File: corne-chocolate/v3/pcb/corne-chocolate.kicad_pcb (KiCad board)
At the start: 2 copper layers, 275.5 x 105.6 mm, 154 parts, among them J1 MJ-4PP-9, J2 OLED, J3 MJ-4PP-9, J4 OLED, SW10 SW_PUSH, SW11 SW_PUSH, SW12 SW_PUSH, SW14 SW_PUSH, SW15 SW_PUSH, SW16 SW_PUSH, SW17 SW_PUSH, SW18 SW_PUSH, SW19 SW_PUSH, SW2 SW_PUSH, SW20 SW_PUSH, SW21 SW_PUSH, SW23 SW_PUSH, SW24 SW_PUSH, SW25 SW_PUSH, SW26 SW_PUSH, SW27 SW_PUSH, SW29 SW_PUSH, SW3 SW_PUSH, SW30 SW_PUSH, SW31 SW_PUSH, SW32 SW_PUSH, SW33 SW_PUSH, SW35 SW_PUSH, SW36 SW_PUSH, SW37 SW_PUSH, SW38 SW_PUSH, SW39 SW_PUSH, SW4 SW_PUSH, SW40 SW_PUSH, SW41 SW_PUSH, SW42 SW_PUSH, SW5 SW_PUSH, SW6 SW_PUSH, SW8 SW_PUSH, SW9 SW_PUSH, U1 ProMicro, U2 ProMicro

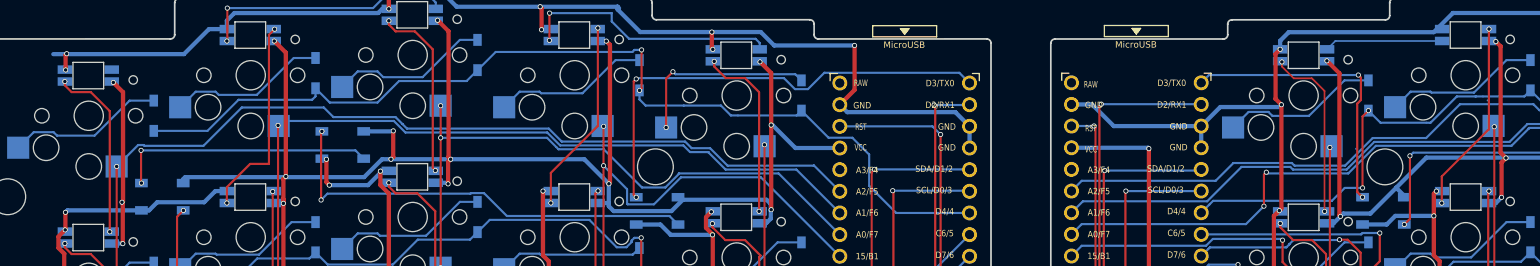
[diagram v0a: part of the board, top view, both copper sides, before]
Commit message: Fix incorrect connections
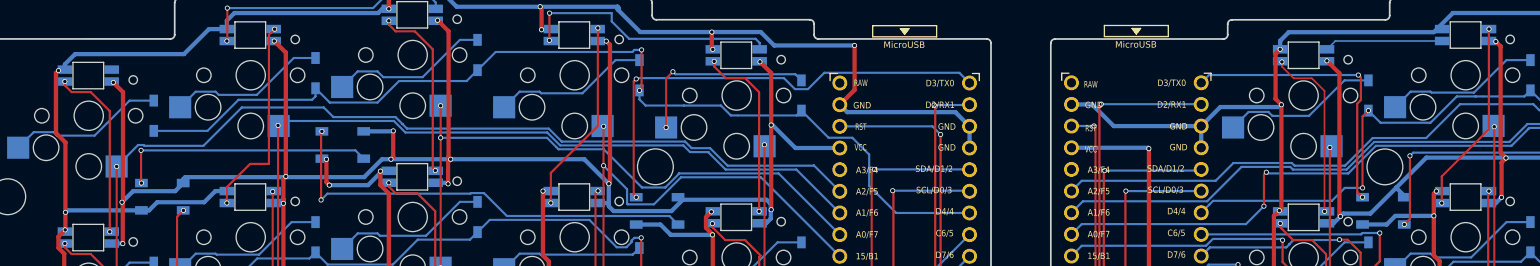
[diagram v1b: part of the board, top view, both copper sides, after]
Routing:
- net GND: track 507.1 -> 522.1 mm, vias 35 -> 34
- net VCC: track 427.1 -> 435.2 mm
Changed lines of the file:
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@@
     (thickness 1.6)
     (drawings 605)
-    (tracks 1983)
+    (tracks 1987)
     (zones 0)
     (modules 154)
@@
     (0 F.Cu signal)
     (31 B.Cu signal)
-    (32 B.Adhes user)
-    (33 F.Adhes user)
-    (34 B.Paste user)
-    (35 F.Paste user)
-    (36 B.SilkS user)
-    (37 F.SilkS user)
-    (38 B.Mask user)
-    (39 F.Mask user)
-    (40 Dwgs.User user)
+    (32 B.Adhes user hide)
+    (33 F.Adhes user hide)
+    (34 B.Paste user hide)
+    (35 F.Paste user hide)
+    (36 B.SilkS user hide)
+    (37 F.SilkS user hide)
+    (38 B.Mask user hide)
+    (39 F.Mask user hide)
+    (40 Dwgs.User user hide)
     (41 Cmts.User user hide)
-    (42 Eco1.User user)
-    (43 Eco2.User user)
-    (44 Edge.Cuts user)
-    (45 Margin user)
-    (46 B.CrtYd user)
-    (47 F.CrtYd user)
-    (48 B.Fab user)
+    (42 Eco1.User user hide)
+    (43 Eco2.User user hide)
+    (44 Edge.Cuts user hide)
+    (45 Margin user hide)
+    (46 B.CrtYd user hide)
+    (47 F.CrtYd user hide)
+    (48 B.Fab user hide)
     (49 F.Fab user hide)
   )
@@
     (effects (font (size 1 1) (thickness 0.125)) (justify left))
   )
+  (via (at 35.56 30.48) (size 0.6) (drill 0.4) (layers F.Cu B.Cu) (net 23))
   (segment (start 122.7075 35.18) (end 122.143681 35.743819) (width 0.25) (layer B.Cu) (net 1))
   (segment (start 103.7075 33.86996) (end 103.7075 32.805) (width 0.25) (layer B.Cu) (net 1))
@@
   (segment (start 108.54522 65.35736) (end 111.6731 65.35736) (width 0.5) (layer B.Cu) (net 23))
   (segment (start 105.44381 62.25595) (end 108.54522 65.35736) (width 0.5) (layer B.Cu) (net 23))
-  (via (at 36.39398 30.40696) (size 0.6) (drill 0.4) (layers F.Cu B.Cu) (net 23))
-  (segment (start 36.35298 30.36596) (end 36.39398 30.40696) (width 0.5) (layer B.Cu) (net 23))
   (segment (start 36.3067 30.36596) (end 36.35298 30.36596) (width 0.5) (layer B.Cu) (net 23))
-  (via (at 36.5218 28.50195) (size 0.6) (drill 0.4) (layers F.Cu B.Cu) (net 23))
-  (segment (start 36.39398 28.62977) (end 36.5218 28.50195) (width 0.5) (layer F.Cu) (net 23))
-  (segment (start 36.39398 30.40696) (end 36.39398 28.62977) (width 0.5) (layer F.Cu) (net 23))
   (via (at 92.2181 25.69272) (size 0.6) (drill 0.4) (layers F.Cu B.Cu) (net 23))
   (segment (start 92.29486 25.61596) (end 92.2181 25.69272) (width 0.5) (layer B.Cu) (net 23))
@@
   (segment (start 113.66634 85.19648) (end 112.64334 84.17348) (width 0.508) (layer B.Cu) (net 23))
   (segment (start 115.61936 85.19648) (end 113.66634 85.19648) (width 0.508) (layer B.Cu) (net 23))
-  (segment (start 34.94806 28.55194) (end 50.2768 28.55194) (width 0.5) (layer B.Cu) (net 23))
+  (segment (start 36.35298 30.36596) (end 36.39398 30.40696) (width 0.5) (layer B.Cu) (net 23))
+  (segment (start 36.3067 29.744697) (end 36.3067 30.36596) (width 0.5) (layer B.Cu) (net 23))
+  (segment (start 37.499457 28.55194) (end 36.3067 29.744697) (width 0.5) (layer B.Cu) (net 23))
+  (segment (start 50.2768 28.55194) (end 37.499457 28.55194) (width 0.5) (layer B.Cu) (net 23))
+  (segment (start 36.37874 38.915238) (end 36.37874 47.11) (width 0.5) (layer F.Cu) (net 23))
+  (segment (start 35.260001 37.796499) (end 36.37874 38.915238) (width 0.5) (layer F.Cu) (net 23))
+  (segment (start 35.260001 30.779999) (end 35.260001 37.796499) (width 0.5) (layer F.Cu) (net 23))
+  (segment (start 35.56 30.48) (end 35.260001 30.779999) (width 0.5) (layer F.Cu) (net 23))
   (segment (start 73.506708 40.88095) (end 71.407698 42.97996) (width 0.5) (layer B.Cu) (net 24))
   (segment (start 118.566702 48.39096) (end 119.106701 47.850961) (width 0.5) (layer B.Cu) (net 24))
@@
   (segment (start 121.02336 81.49248) (end 120.51936 81.99648) (width 0.508) (layer B.Cu) (net 24))
   (segment (start 133.8345 81.49248) (end 121.02336 81.49248) (width 0.508) (layer B.Cu) (net 24))
+  (segment (start 44.307498 44.626121) (end 43.0075 45.926119) (width 0.5) (layer B.Cu) (net 24))
+  (segment (start 49.237619 44.626121) (end 44.307498 44.626121) (width 0.5) (layer B.Cu) (net 24))
+  (segment (start 50.18762 43.67612) (end 49.237619 44.626121) (width 0.5) (layer B.Cu) (net 24))
   (via (at 42.6627 79.9014) (size 0.6) (drill 0.4) (layers F.Cu B.Cu) (net 26))
   (segment (start 42.4913 79.73) (end 42.6627 79.9014) (width 0.25) (layer B.Cu) (net 26))
@@
   (segment (start 154.39042 36.98048) (end 154.3789 36.992) (width 0.254) (layer B.Cu) (net 67))
   (segment (start 157.024419 36.98048) (end 154.39042 36.98048) (width 0.254) (layer B.Cu) (net 67))
-  (segment (start 187.7729 39.653202) (end 187.807818 39.653202) (width 0.254) (layer B.Cu) (net 68))
-  (segment (start 203.203459 33.970521) (end 203.207459 33.966521) (width 0.254) (layer B.Cu) (net 68))
   (via (at 261.20938 41.78108) (size 0.6) (drill 0.4) (layers F.Cu B.Cu) (net 69))
   (segment (start 261.1533 41.725) (end 261.20938 41.78108) (width 0.25) (layer B.Cu) (net 69))

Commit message: Fix boundaries and add "JLCJLCJLCJLC"
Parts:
- removed the REF** at (238.7, 83.2)
- removed the REF** at (276.7, 83.2)
- removed the REF** at (58.1, 83.2)
- removed the REF** at (20.2, 83.2)
- added REF**: Breakaway_Tabs, kbd:Breakaway_Tabs, F.Cu at (237.5, 83.0)
- added REF**: Breakaway_Tabs, kbd:Breakaway_Tabs, F.Cu at (257.8, 83.0)
- added REF**: Breakaway_Tabs, kbd:Breakaway_Tabs, F.Cu at (59.7, 83.0)
- added REF**: Breakaway_Tabs, kbd:Breakaway_Tabs, F.Cu at (39.4, 83.0)
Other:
- board size 275.5 x 105.6 mm -> 241.3 x 104.1 mm
- board text added: "JLCJLCJLCJLC"

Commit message: Clean up PCB
- Relabeled LEDs and switch numbers
- Added dimensions back in
- Updated the title/comments
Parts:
- renumbered LED11 to LED10, LED12 to LED11, LED14 to LED12, LED15 to LED13, LED16 to LED14, LED17 to LED15, LED18 to LED16, LED20 to LED17, LED21 to LED18, LED22 to LED19, LED23 to LED20, LED24 to LED21, LED25 to LED22, LED26 to LED23, LED27 to LED24, LED28 to LED25, LED29 to LED26, LED30 to LED27, LED31 to LED28, LED32 to LED29, LED33 to LED30, LED35 to LED31, LED36 to LED32, LED37 to LED33, LED38 to LED34, LED39 to LED35, LED41 to LED36, LED42 to LED37, LED43 to LED38, LED44 to LED39, LED45 to LED40, LED47 to LED41, LED48 to LED42, LED49 to LED43, LED50 to LED44, LED51 to LED45, LED52 to LED46, LED53 to LED47, LED54 to LED48, LED8 to LED7, LED9 to LED8, LED10 to LED9, SW2 to SW1, SW12 to SW10, SW14 to SW11, SW15 to SW12, SW16 to SW13, SW17 to SW14, SW18 to SW15, SW19 to SW16, SW20 to SW17, SW21 to SW18, SW23 to SW19, SW3 to SW2, SW24 to SW20, SW25 to SW21, SW26 to SW22, SW27 to SW23, SW29 to SW24, SW30 to SW25, SW31 to SW26, SW32 to SW27, SW33 to SW28, SW35 to SW29, SW4 to SW3, SW36 to SW30, SW37 to SW31, SW38 to SW32, SW39 to SW33, SW40 to SW34, SW41 to SW35, SW42 to SW36, SW5 to SW4, SW6 to SW5, SW8 to SW6, SW9 to SW7, SW10 to SW8, SW11 to SW9
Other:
- board size 241.3 x 104.1 mm -> 240 x 104.1 mm

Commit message: Round all corners and delete extra trace
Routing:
- net GNDA: track 492.8 -> 476.8 mm, vias 31 -> 30
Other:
- outline, holes or cut-outs redrawn
